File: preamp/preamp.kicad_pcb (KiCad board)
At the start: 2 copper layers, 63 x 27.4 mm, 20 parts, among them J1 XLR3_AudioJack2_Combo, J2 RCJ-22, U1 SSM2019

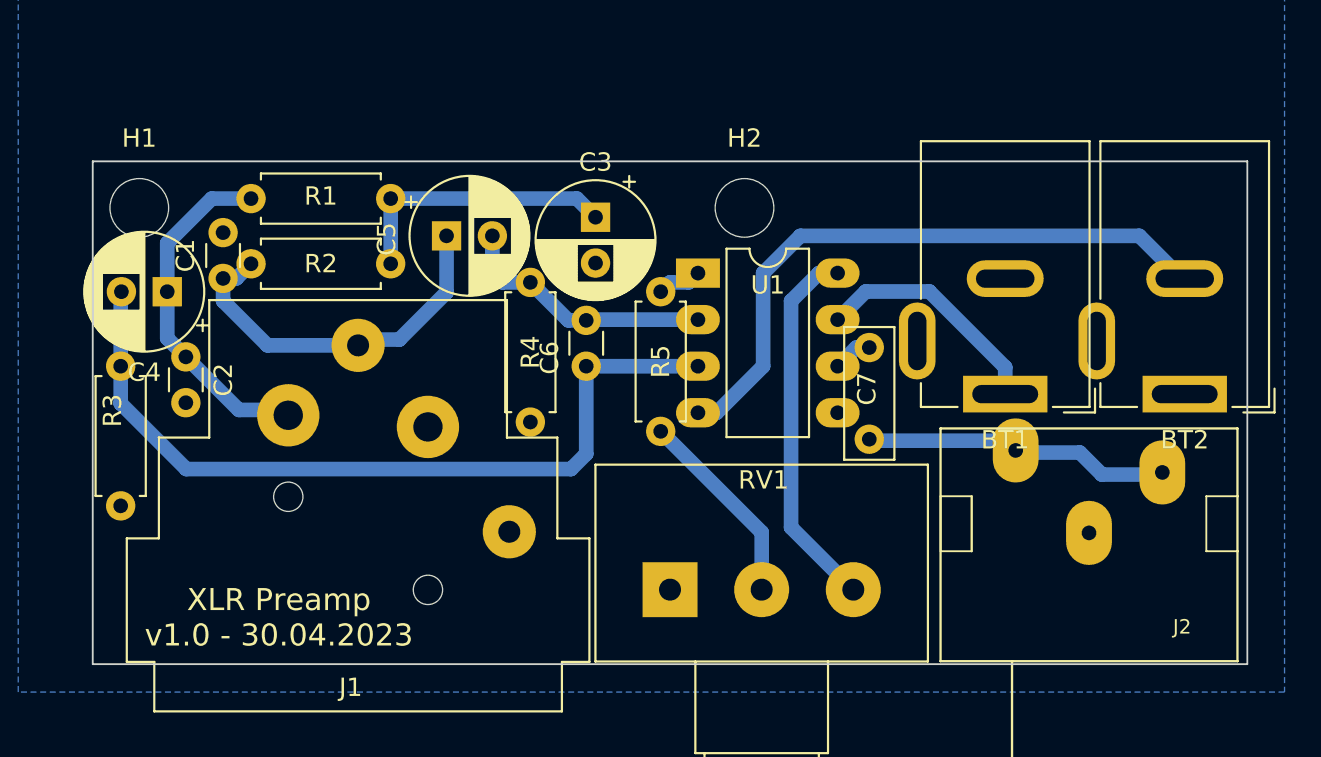
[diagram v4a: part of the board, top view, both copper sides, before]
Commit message: Add mounting holes
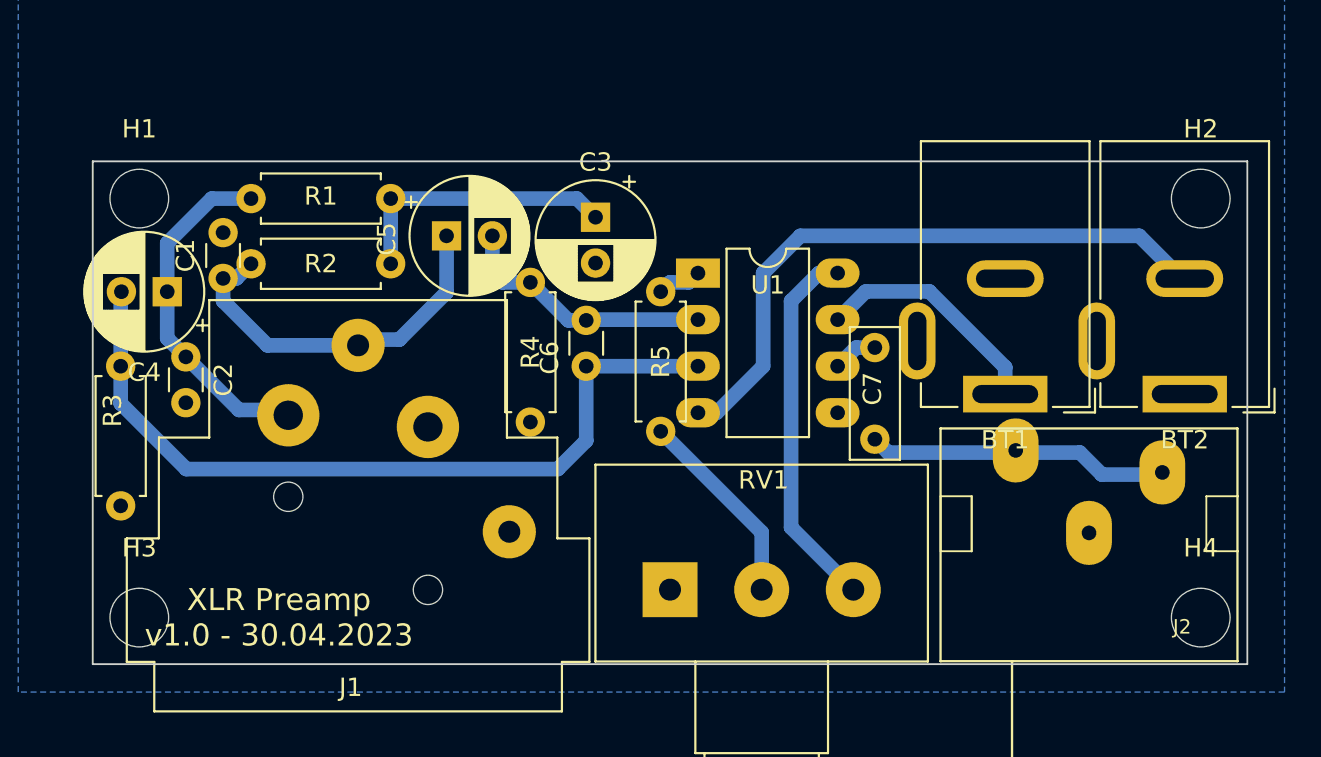
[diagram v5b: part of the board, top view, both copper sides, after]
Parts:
- added H3: MountingHole, MountingHole:MountingHole_3.2mm_M3_DIN965, F.Cu at (98.0, 95.5)
- added H4: MountingHole, MountingHole:MountingHole_3.2mm_M3_DIN965, F.Cu at (156.0, 95.5)
- moved H2 24.9 mm to (156.0, 72.6)
- moved H1 0.51 mm to (98.0, 72.6)
- moved C7 0.30 mm to (138.2, 80.8)
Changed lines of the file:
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@@
   (net 14 "Net-(C7-Pad2)")
   (footprint "MountingHole:MountingHole_3.2mm_M3_DIN965" (layer "F.Cu")
-    (at 98.044 73.152)
+    (at 98.044 72.644)
     (descr "Mounting Hole 3.2mm, no annular, M3, DIN965")
     (tags "mounting hole 3.2mm no annular m3 din965")
@@
     (fp_circle (center 0 0) (end 2.8 0) (layer "Cmts.User") (width 0.15) (fill none))
     (fp_circle (center 0 0) (end 3.05 0) (layer "F.CrtYd") (width 0.05) (fill none))
+    (pad "" np_thru_hole circle (at 0 0) (size 3.2 3.2) (drill 3.2) (layers *.Cu *.Mask))
+    (pad "" np_thru_hole circle (at 0 0) (size 3.2 3.2) (drill 3.2) (layers *.Cu *.Mask))
+  )
+  (footprint "MountingHole:MountingHole_3.2mm_M3_DIN965" (layer "F.Cu")
+    (at 155.956 95.504)
+    (descr "Mounting Hole 3.2mm, no annular, M3, DIN965")
+    (tags "mounting hole 3.2mm no annular m3 din965")
+    (property "Sheetfile" "preamp.kicad_sch")
+    (property "Sheetname" "")
+    (attr exclude_from_pos_files)
+    (fp_text reference "H4" (at 0 -3.8) (layer "F.SilkS")
+      (effects (font (size 1 1) (thickness 0.15)))
+    )
+    (fp_text value "MountingHole" (at 0 3.8) (layer "F.Fab")
+      (effects (font (size 1 1) (thickness 0.15)))
+    )
+    (fp_text user "${REFERENCE}" (at 0 0) (layer "F.Fab")
+      (effects (font (size 1 1) (thickness 0.15)))
+    )
+    (fp_circle (center 0 0) (end 2.8 0) (layer "Cmts.User") (width 0.15) (fill none))
+    (fp_circle (center 0 0) (end 3.05 0) (layer "F.CrtYd") (width 0.05) (fill none))
+    (pad "" np_thru_hole circle (at 0 0) (size 3.2 3.2) (drill 3.2) (layers *.Cu *.Mask))
     (pad "" np_thru_hole circle (at 0 0) (size 3.2 3.2) (drill 3.2) (layers *.Cu *.Mask))
   )
@@
   )
   (footprint "Capacitor_THT:C_Rect_L7.0mm_W2.5mm_P5.00mm" (layer "F.Cu")
-    (at 137.8712 80.772 -90)
+    (at 138.176 80.772 -90)
     (descr "C, Rect series, Radial, pin pitch=5.00mm, , length*width=7*2.5mm^2, Capacitor")
     (tags "C Rect series Radial pin pitch 5.00mm  length 7mm width 2.5mm Capacitor")
@@
   )
   (footprint "MountingHole:MountingHole_3.2mm_M3_DIN965" (layer "F.Cu")
-    (at 131.064 73.152)
+    (at 155.956 72.644)
     (descr "Mounting Hole 3.2mm, no annular, M3, DIN965")
     (tags "mounting hole 3.2mm no annular m3 din965")
@@
     (fp_circle (center 0 0) (end 2.8 0) (layer "Cmts.User") (width 0.15) (fill none))
     (fp_circle (center 0 0) (end 3.05 0) (layer "F.CrtYd") (width 0.05) (fill none))
+    (pad "" np_thru_hole circle (at 0 0) (size 3.2 3.2) (drill 3.2) (layers *.Cu *.Mask))
     (pad "" np_thru_hole circle (at 0 0) (size 3.2 3.2) (drill 3.2) (layers *.Cu *.Mask))
   )
@@
     )
   )
+  (footprint "MountingHole:MountingHole_3.2mm_M3_DIN965" (layer "F.Cu")
+    (at 98.044 95.504)
+    (descr "Mounting Hole 3.2mm, no annular, M3, DIN965")
+    (tags "mounting hole 3.2mm no annular m3 din965")
+    (property "Sheetfile" "preamp.kicad_sch")
+    (property "Sheetname" "")
+    (attr exclude_from_pos_files)
+    (fp_text reference "H3" (at 0 -3.8) (layer "F.SilkS")
+      (effects (font (size 1 1) (thickness 0.15)))
+    )
+    (fp_text value "MountingHole" (at 0 3.8) (layer "F.Fab")
+      (effects (font (size 1 1) (thickness 0.15)))
+    )
+    (fp_text user "${REFERENCE}" (at 0 0) (layer "F.Fab")
+      (effects (font (size 1 1) (thickness 0.15)))
+    )
+    (fp_circle (center 0 0) (end 2.8 0) (layer "Cmts.User") (width 0.15) (fill none))
+    (fp_circle (center 0 0) (end 3.05 0) (layer "F.CrtYd") (width 0.05) (fill none))
+    (pad "" np_thru_hole circle (at 0 0) (size 3.2 3.2) (drill 3.2) (layers *.Cu *.Mask))
+    (pad "" np_thru_hole circle (at 0 0) (size 3.2 3.2) (drill 3.2) (layers *.Cu *.Mask))
+  )
   (gr_rect (start 95.504 70.612) (end 158.496 98.044) (layer "Edge.Cuts") (width 0.1) (fill none))
   (gr_text "XLR Preamp\nv1.0 - 30.04.2023" (at 105.664 95.504) (layer "F.SilkS")
@@
   (segment (start 122.428 81.788) (end 128.524 81.788) (width 0.8) (layer "B.Cu") (net 5))
   (segment (start 97.028 77.764) (end 97.028 83.82) (width 0.8) (layer "B.Cu") (net 5))
-  (segment (start 121.598937 87.401823) (end 122.428 86.57276) (width 0.8) (layer "B.Cu") (net 5))
-  (segment (start 100.609823 87.401823) (end 121.598937 87.401823) (width 0.8) (layer "B.Cu") (net 5))
+  (segment (start 122.428 85.852) (end 122.428 81.788) (width 0.8) (layer "B.Cu") (net 5))
+  (segment (start 100.609823 87.401823) (end 120.878177 87.401823) (width 0.8) (layer "B.Cu") (net 5))
+  (segment (start 120.878177 87.401823) (end 122.428 85.852) (width 0.8) (layer "B.Cu") (net 5))
   (segment (start 97.028 83.82) (end 100.609823 87.401823) (width 0.8) (layer "B.Cu") (net 5))
   (segment (start 97.068 77.724) (end 97.028 77.764) (width 0.8) (layer "B.Cu") (net 5))
-  (segment (start 122.428 86.57276) (end 122.428 81.788) (width 0.8) (layer "B.Cu") (net 5))
   (segment (start 122.468 79.248) (end 128.524 79.248) (width 0.8) (layer "B.Cu") (net 6))
   (segment (start 119.38 77.216) (end 117.856 77.216) (width 0.8) (layer "B.Cu") (net 6))
@@
   (segment (start 133.604 78.232) (end 133.604 90.584) (width 0.8) (layer "B.Cu") (net 12))
   (segment (start 136.144 81.788) (end 137.16 80.772) (width 0.8) (layer "B.Cu") (net 13))
-  (segment (start 137.16 80.772) (end 137.8712 80.772) (width 0.8) (layer "B.Cu") (net 13))
-  (segment (start 137.9512 85.852) (end 145.212 85.852) (width 0.8) (layer "B.Cu") (net 14))
-  (segment (start 145.86 86.5) (end 149.36 86.5) (width 0.8) (layer "B.Cu") (net 14))
+  (segment (start 137.16 80.772) (end 138.176 80.772) (width 0.8) (layer "B.Cu") (net 13))
+  (segment (start 138.176 85.772) (end 138.904 86.5) (width 0.8) (layer "B.Cu") (net 14))
+  (segment (start 149.36 86.5) (end 150.56 87.7) (width 0.8) (layer "B.Cu") (net 14))
+  (segment (start 138.904 86.5) (end 149.36 86.5) (width 0.8) (layer "B.Cu") (net 14))
   (segment (start 150.56 87.7) (end 153.86 87.7) (width 0.8) (layer "B.Cu") (net 14))
-  (segment (start 145.212 85.852) (end 145.86 86.5) (width 0.8) (layer "B.Cu") (net 14))
-  (segment (start 137.8712 85.772) (end 137.9512 85.852) (width 0.8) (layer "B.Cu") (net 14))
-  (segment (start 149.36 86.5) (end 150.56 87.7) (width 0.8) (layer "B.Cu") (net 14))
   (zone (net 2) (net_name "GNDA") (layer "B.Cu") (hatch edge 0.508)
     (connect_pads (clearance 0.1))

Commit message: Prepare for milling
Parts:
- moved C3 1.83 mm to (124.5, 72.6)
- moved R2 1.61 mm to (113.3, 75.7)
- moved C5 1.61 mm to (116.3, 74.2)
- moved R1 1.52 mm to (105.7, 72.6)
- moved R5 1.02 mm to (125.5, 85.3)
- moved C7 0.15 mm to (138.3, 80.9)
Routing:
- net Net-(C1-Pad1): track 20.6 -> 24.3 mm
- net Net-(C2-Pad1): track 19.1 -> 20.9 mm
- net Net-(R5-Pad1): track 10.9 -> 11.9 mm
- net Net-(R5-Pad2): track 2.45 -> 3.47 mm
- net +15V: track 13.0 -> 13.7 mm
- net Net-(C5-Pad2): track 14.3 -> 13.7 mm
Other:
- board text added: "XLR Preamp - v1.0 - 30.04.2023"
- board text removed: "XLR Preamp v1.0 - 30.04.2023"

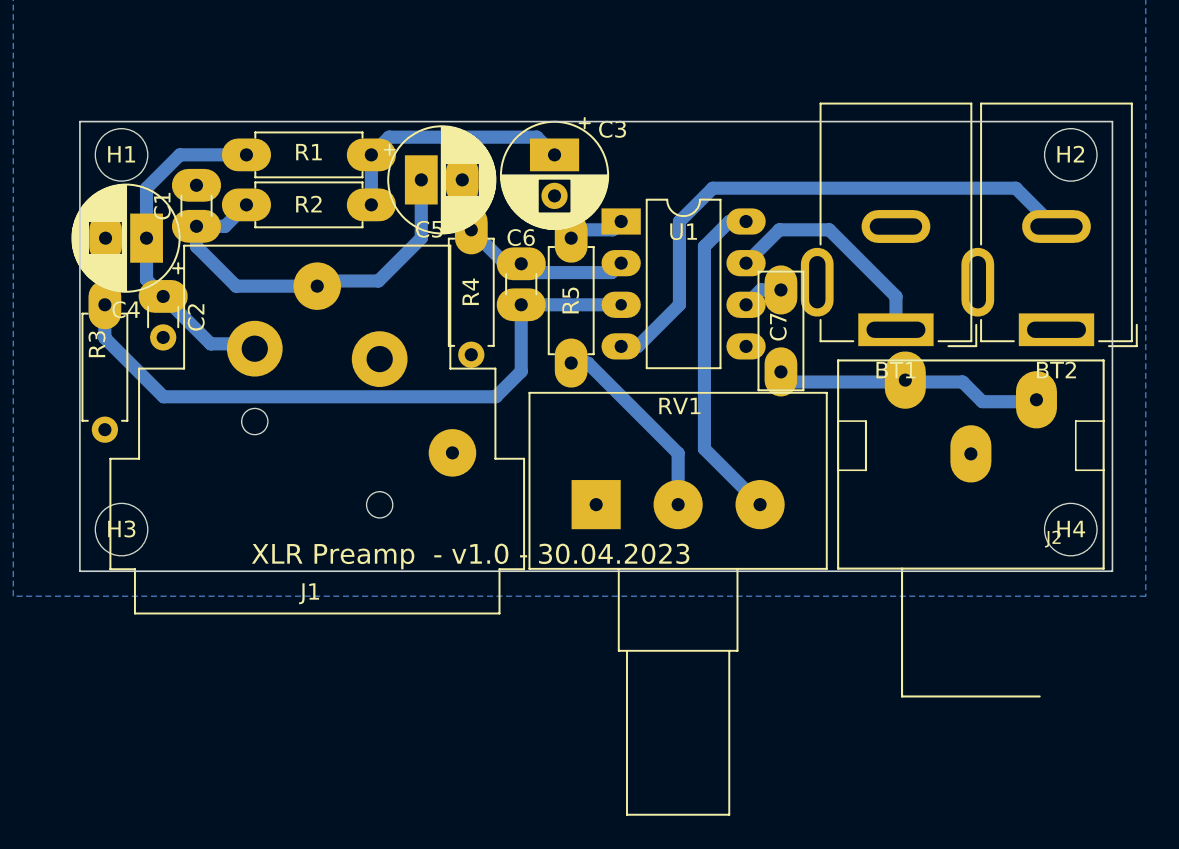
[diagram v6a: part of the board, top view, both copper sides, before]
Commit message: Update board with the findings of the pcb
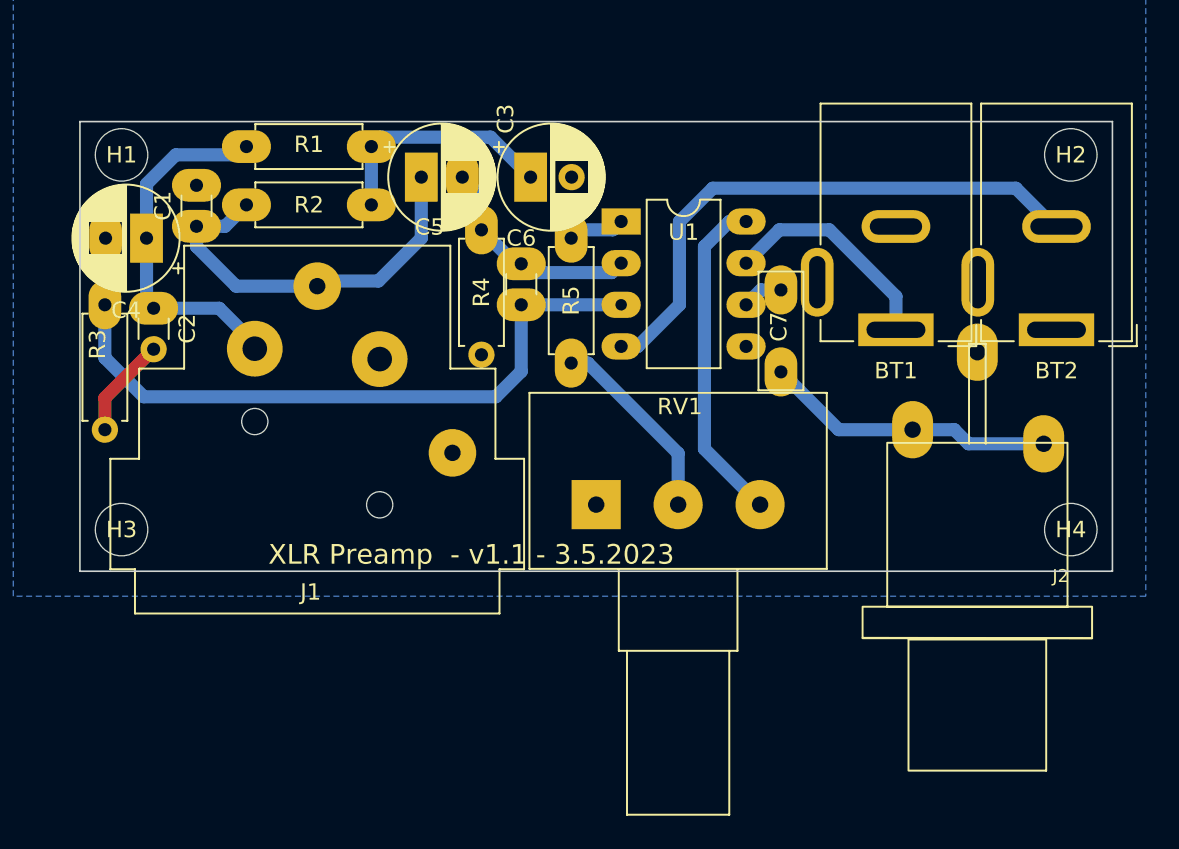
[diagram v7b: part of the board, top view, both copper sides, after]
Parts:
- moved J2 2.36 mm to (150.3, 90.2)
- moved C3 1.99 mm to (123.0, 74.0), turned to 0 degrees
- moved C2 0.93 mm to (100.0, 82.0)
- moved R4 0.62 mm to (120.0, 84.8)
- moved R1 0.51 mm to (105.7, 72.1)
- moved C5 0.17 mm to (116.3, 74.0)
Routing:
- net GNDA: track 0.00 -> 6.14 mm
- net Net-(C7-Pad2): track 16.3 -> 17.8 mm
- net Net-(C2-Pad1): track 20.9 -> 22.2 mm
- net Net-(C4-Pad2): track 43.8 -> 44.5 mm
- net Net-(C3-Pad1): track 15.1 -> 14.5 mm
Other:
- board text added: "XLR Preamp - v1.1 - 3.5.2023"
- board text removed: "XLR Preamp - v1.0 - 30.04.2023"

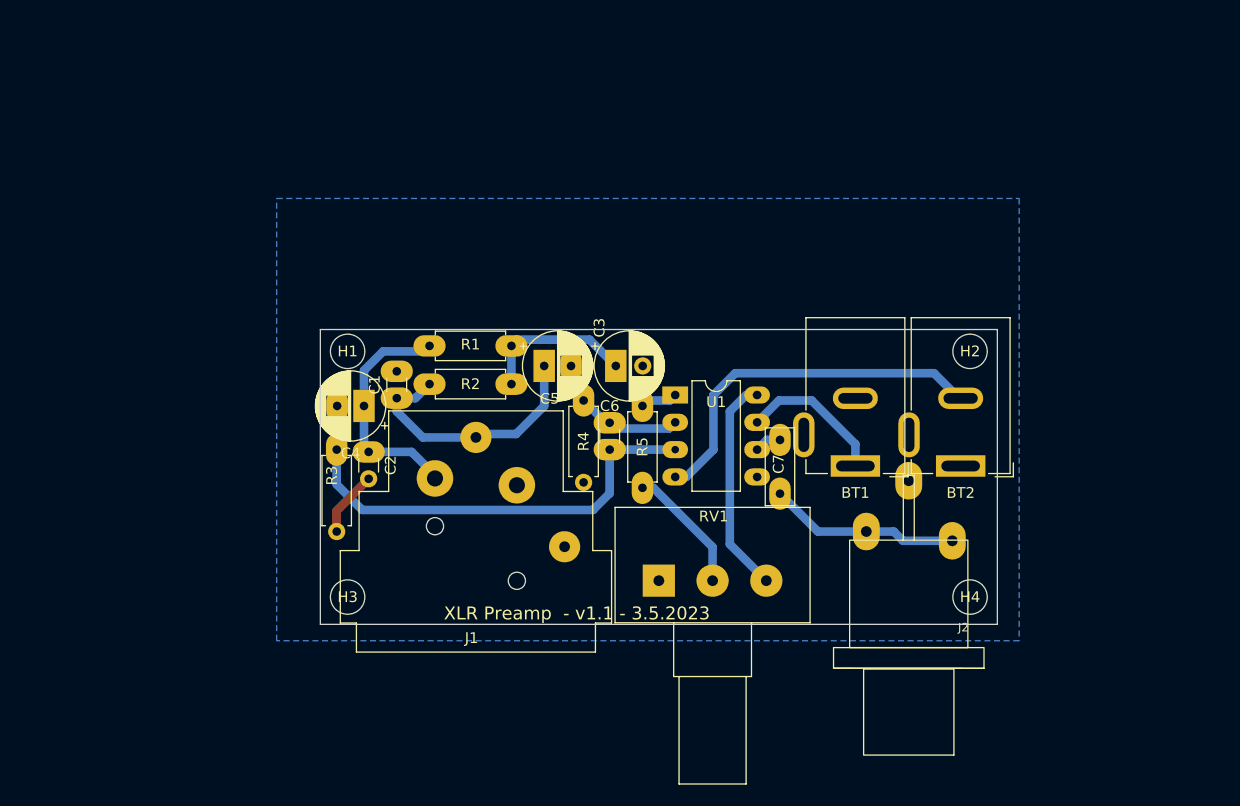
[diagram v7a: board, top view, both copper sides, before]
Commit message: Replace the RCA jack with an Audio Jack
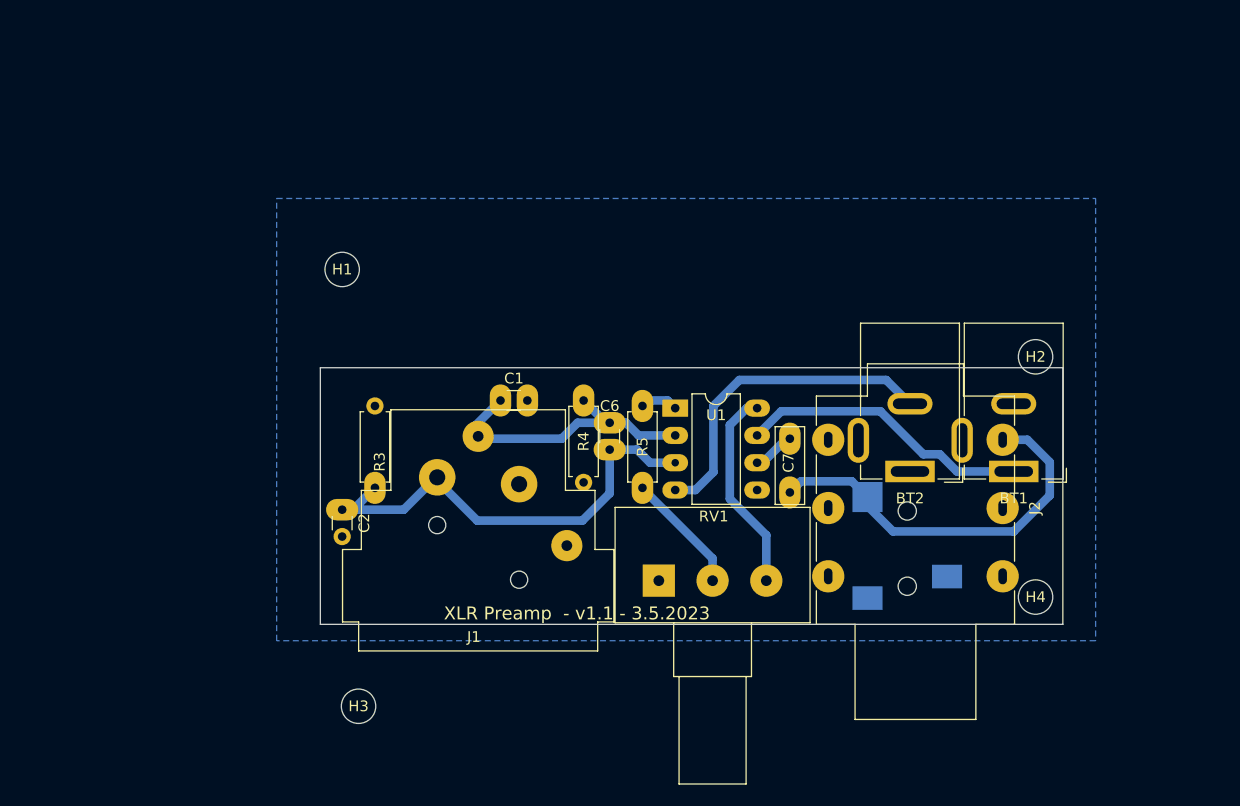
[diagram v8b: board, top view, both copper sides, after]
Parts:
- removed C3, C4, C5: 47u, Capacitor_THT:CP_Radial_D6.3mm_P2.50mm
- removed R1, R2: 2k2, Resistor_THT:R_Axial_DIN0207_L6.3mm_D2.5mm_P7.62mm_Horizontal
- added J3: AudioJack2, Connector_Audio:Jack_3.5mm_CUI_SJ-3523-SMT_Horizontal, B.Cu at (150.1, 92.0)
- C1, C2: value 470p -> 100p
- C6: value 200p -> 180p
- J2: value RCJ-22 -> AudioJack2; footprint rcj-22:rcj-22 -> Connector_Audio:Jack_6.35mm_Neutrik_NMJ6HFD2-AU_Horizontal
- R3, R4: value 2k2 -> 10k
- RV1: value 5k -> 2k5
- moved BT1 14.7 mm to (160.0, 83.8)
- moved J2 12.8 mm to (159.0, 80.9), turned to -90 degrees
- moved H3 10.2 mm to (99.1, 105.7)
- moved C1 9.65 mm to (112.3, 77.2), turned to 0 degrees
- moved H1 7.64 mm to (97.5, 65.0)
- moved H2 6.12 mm to (162.1, 73.2)
- moved H4 6.10 mm to (162.1, 95.5)
- moved C2 5.91 mm to (97.5, 87.4)
- moved R3 5.03 mm to (100.6, 85.3), turned to 90 degrees
- moved BT2 4.74 mm to (150.4, 83.8)
- moved U1 1.22 mm to (128.5, 77.9)
- moved C7 0.93 mm to (139.2, 80.8)
- moved J1 0.23 mm to (114.0, 85.0)
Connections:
- C6 pad 1: Net-(C4-Pad2) -> Net-(C2-Pad1)
- C6 pad 2: Net-(C5-Pad2) -> Net-(C1-Pad1)
- R3 pad 1: Net-(C4-Pad2) -> Net-(C2-Pad1)
- R4 pad 2: Net-(C5-Pad2) -> Net-(C1-Pad1)
- U1 pad 2: Net-(C5-Pad2) -> Net-(C1-Pad1)
- U1 pad 3: Net-(C4-Pad2) -> Net-(C2-Pad1)
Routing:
- net Net-(C4-Pad2): track 44.5 -> 0.00 mm
- net Net-(C2-Pad1): track 22.2 -> 43.3 mm
- net Net-(C7-Pad2): track 17.8 -> 36.8 mm
- net Net-(C3-Pad1): track 14.5 -> 0.00 mm
- net Net-(C5-Pad2): track 13.5 -> 0.00 mm
- net +15V: track 13.7 -> 27.1 mm
- net GNDA: track 6.14 -> 0.00 mm
- net -15V: track 34.4 -> 30.6 mm
- net Net-(C1-Pad1): track 24.5 -> 27.4 mm
- net Net-(C7-Pad1): track 2.50 -> 3.97 mm
- net Net-(RV1-Pad3): track 20.3 -> 19.1 mm
- net Net-(R5-Pad1): track 11.9 -> 11.3 mm
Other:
- board size 63 x 27.4 mm -> 69.1 x 23.9 mm
